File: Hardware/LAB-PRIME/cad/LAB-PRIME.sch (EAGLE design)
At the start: 48 parts, among them IC1 MT48LC16M16A2, IC2 25AA080SN, IC3 MT29F8G08DAA, IC4 FT232RL, U1 STM32F429IGT, U13 MAX4376, U2 LTC1982ES6PBF, U3 DMG6968U-7, U4 TPS62240DDC, U50 MCP601R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

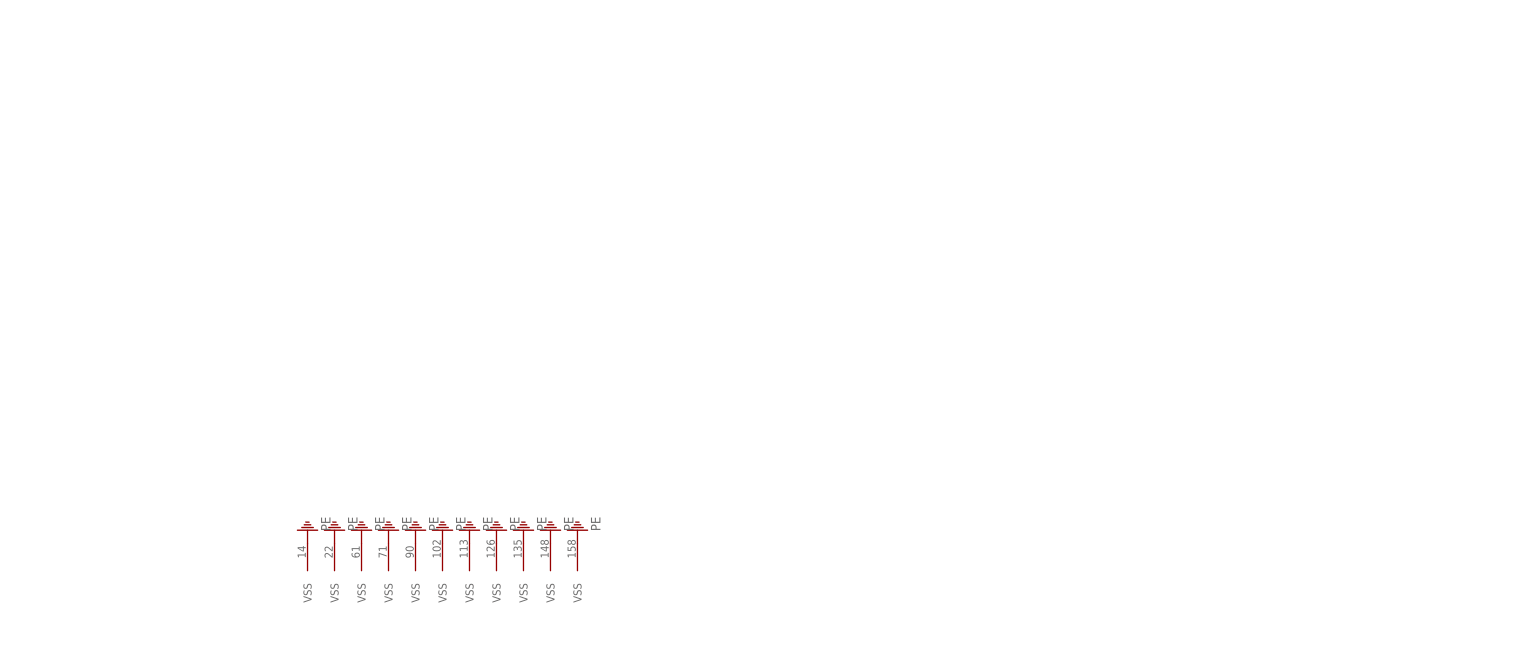
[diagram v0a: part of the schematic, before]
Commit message: 1) Adding the ADSM300F to the LAB304 library 2) Quick updates to the prime board -- spacing related, preliminary 3) Fixing some library pointers in the PPS330D project file
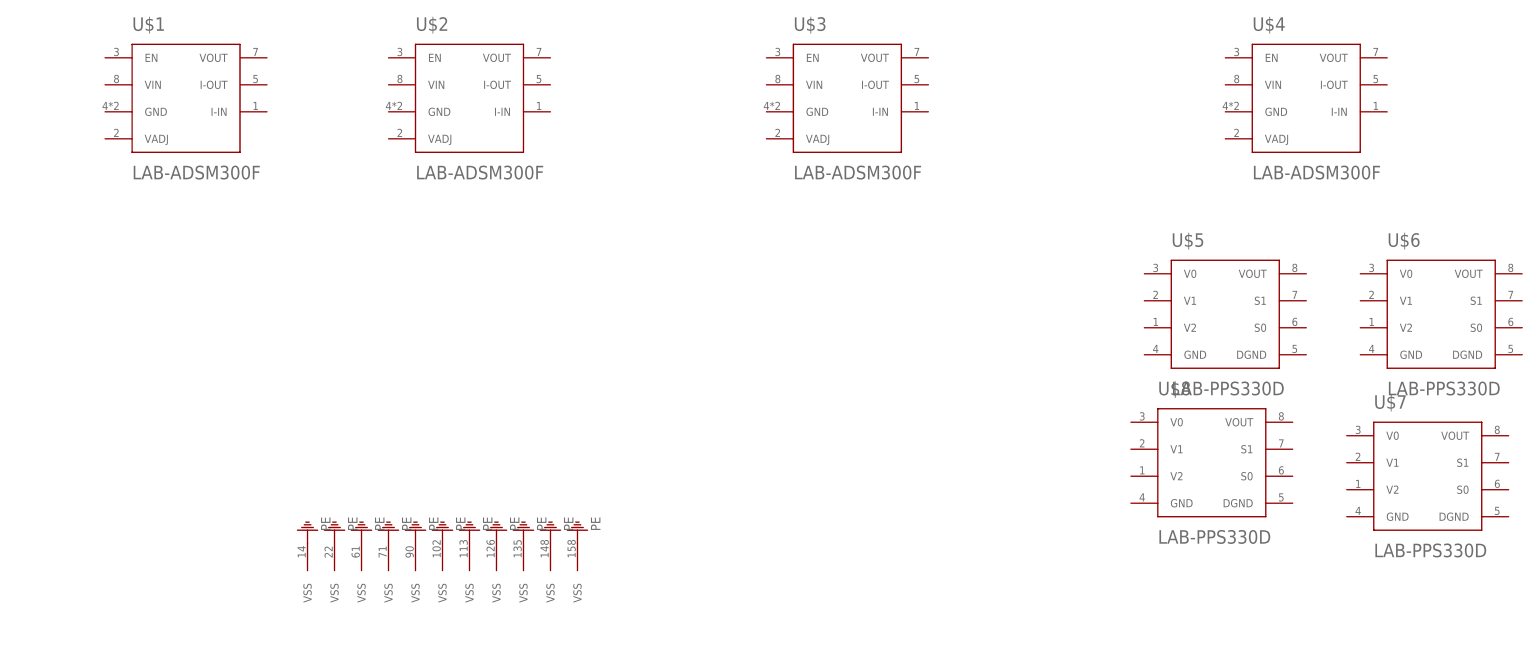
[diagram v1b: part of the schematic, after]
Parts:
- added U$1, U$2, U$3, U$4: LAB-ADSM300F, LAB304:LAB-ADSM300F
- added U$5, U$6, U$7, U$8: LAB-PPS330D, LAB304:LAB-PPS330D
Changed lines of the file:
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@@
 <part name="IC3" library="memory-micron" deviceset="MT29F8G08DAA" device=""/>
 <part name="IC4" library="ftdichip" deviceset="FT232R" device="L"/>
+<part name="U$1" library="LAB304" deviceset="LAB-ADSM300F" device=""/>
+<part name="U$2" library="LAB304" deviceset="LAB-ADSM300F" device=""/>
+<part name="U$3" library="LAB304" deviceset="LAB-ADSM300F" device=""/>
+<part name="U$4" library="LAB304" deviceset="LAB-ADSM300F" device=""/>
+<part name="U$5" library="LAB304" deviceset="LAB-PPS330D" device=""/>
+<part name="U$6" library="LAB304" deviceset="LAB-PPS330D" device=""/>
+<part name="U$7" library="LAB304" deviceset="LAB-PPS330D" device=""/>
+<part name="U$8" library="LAB304" deviceset="LAB-PPS330D" device=""/>
 </parts>
 <sheets>
@@
 <instance part="IC3" gate="G$1" x="566.42" y="208.28"/>
 <instance part="IC4" gate="1" x="523.24" y="276.86"/>
+<instance part="U$1" gate="G$1" x="353.06" y="518.16"/>
+<instance part="U$2" gate="G$1" x="406.4" y="518.16"/>
+<instance part="U$3" gate="G$1" x="477.52" y="518.16"/>
+<instance part="U$4" gate="G$1" x="563.88" y="518.16"/>
+<instance part="U$5" gate="G$1" x="548.64" y="477.52"/>
+<instance part="U$6" gate="G$1" x="589.28" y="477.52"/>
+<instance part="U$7" gate="G$1" x="586.74" y="447.04"/>
+<instance part="U$8" gate="G$1" x="546.1" y="449.58"/>
 </instances>
 <busses>
